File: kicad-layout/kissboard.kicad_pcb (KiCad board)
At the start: 2 copper layers, 132.3 x 103.7 mm, 27 parts, among them J1 Conn_01x04, K1 KEYSW, K10 KEYSW, K11 KEYSW, K12 KEYSW, K13 KEYSW, K14 KEYSW, K15 KEYSW, K16 KEYSW, K17 KEYSW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

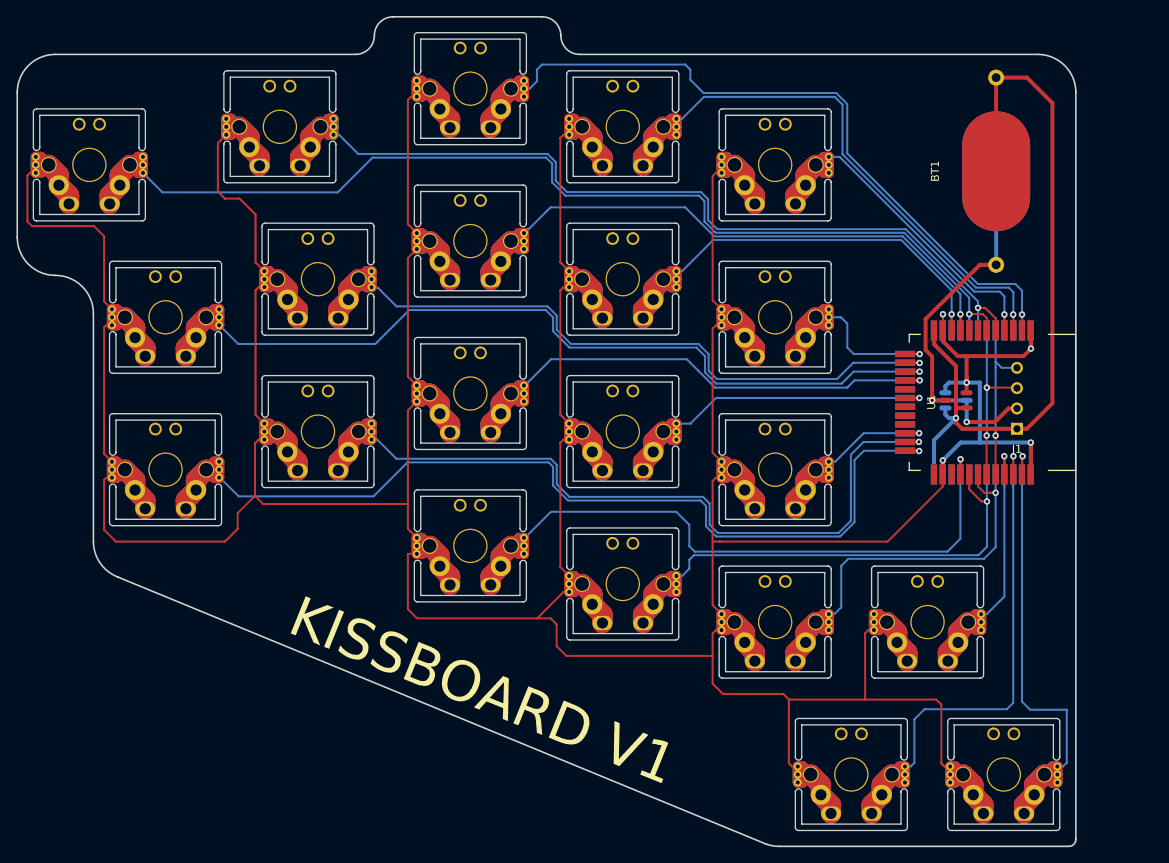
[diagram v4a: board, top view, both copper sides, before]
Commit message: Layout adjusted: lower pinky finger column and straight thumb row
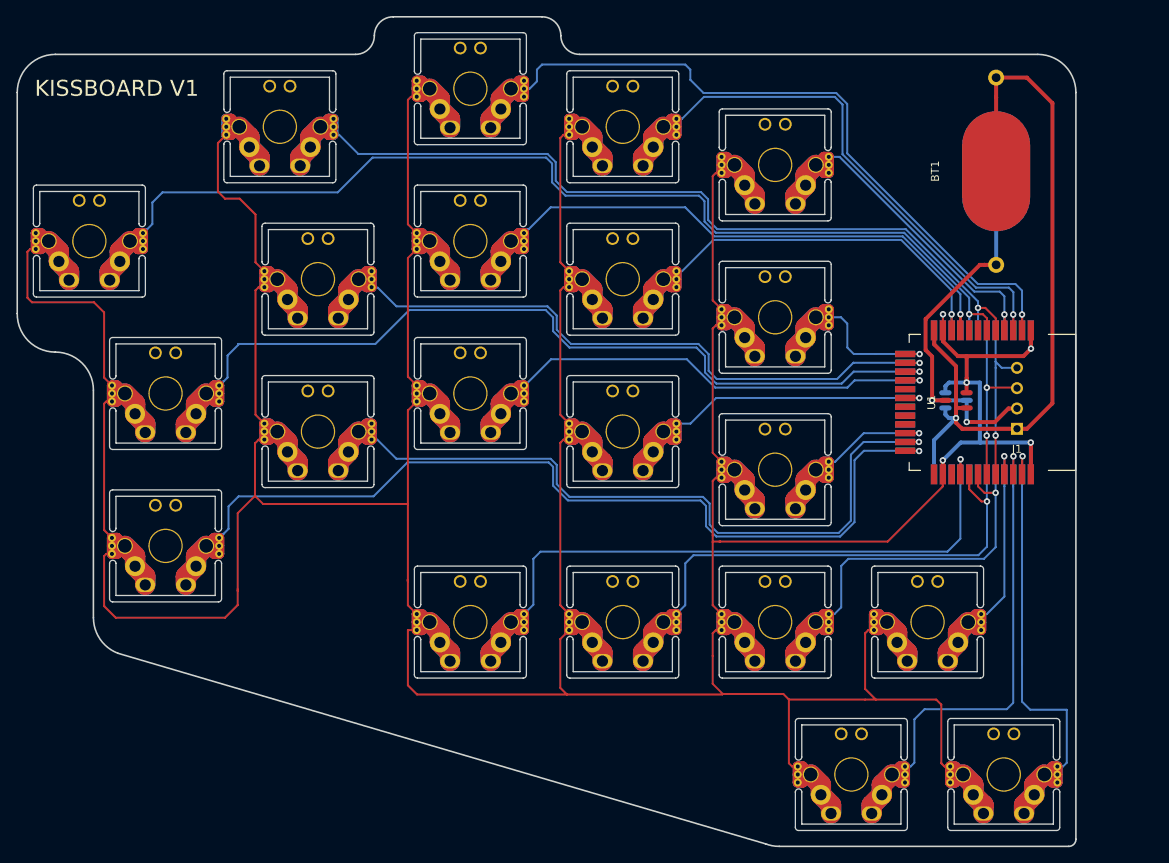
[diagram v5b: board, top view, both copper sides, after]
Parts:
- moved K11 9.53 mm to (52.4, 88.1)
- moved K6 9.53 mm to (52.4, 69.1)
- moved K1 9.52 mm to (42.9, 50.0)
- moved K16 9.52 mm to (90.5, 97.6)
- moved K17 4.76 mm to (109.5, 97.6)
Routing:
- net GND: track 1093.8 -> 1119.8 mm
- net /S17: track 82.0 -> 86.4 mm
- net /S11: track 134.9 -> 137.8 mm
- net /S6: track 125.9 -> 128.8 mm
- net /S1: track 153.5 -> 156.2 mm
- net /S16: track 101.3 -> 103.0 mm
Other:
- outline, holes or cut-outs redrawn

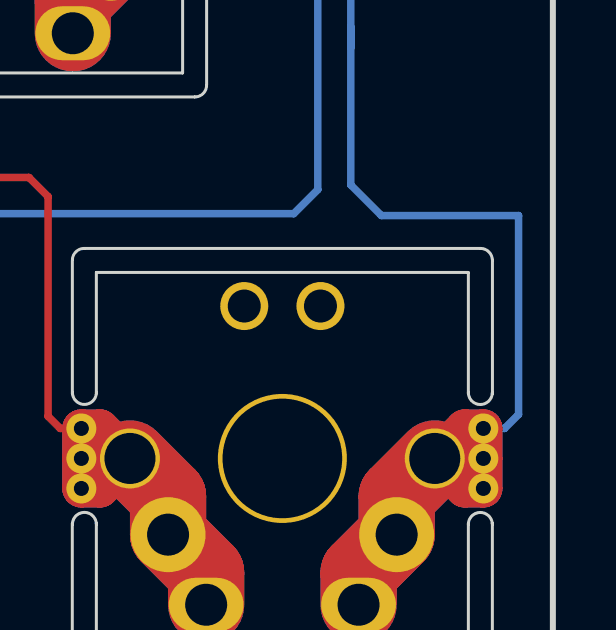
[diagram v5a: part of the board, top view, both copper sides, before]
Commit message: tiny adjustment of a single track
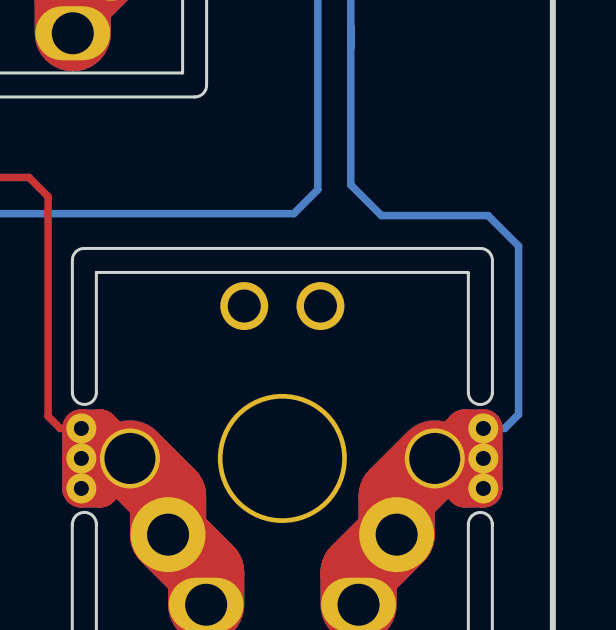
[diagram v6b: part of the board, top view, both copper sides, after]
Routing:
- net /S21: track 74.9 -> 74.3 mm
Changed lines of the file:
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@@
     (thickness 1.6)
     (drawings 21)
-    (tracks 1381)
+    (tracks 1382)
     (zones 0)
     (modules 27)
@@
   (segment (start 154.176998 52.975) (end 154.795787 52.975) (width 0.5) (layer F.Cu) (net 30))
   (segment (start 154.795787 52.975) (end 156.21 52.975) (width 0.5) (layer F.Cu) (net 30))
+  (segment (start 165.0365 109.601) (end 164.0205 108.585) (width 0.25) (layer B.Cu) (net 31))
+  (segment (start 164.0205 108.585) (end 160.4645 108.585) (width 0.25) (layer B.Cu) (net 31))
+  (segment (start 165.0365 115.214356) (end 165.0365 109.601) (width 0.25) (layer B.Cu) (net 31))
   (segment (start 144.86904 68.51396) (end 144.8655 68.5175) (width 0.25) (layer F.Cu) (net 39))
   (segment (start 97.1875 31.95625) (end 96.5675 31.95625) (width 1.27) (layer F.Cu) (net 4))
@@
   (segment (start 160.4645 108.585) (end 159.4435 107.564) (width 0.25) (layer B.Cu) (net 31))
   (segment (start 159.4435 107.564) (end 159.4435 102.2985) (width 0.25) (layer B.Cu) (net 31))
-  (segment (start 165.0365 108.585) (end 160.4645 108.585) (width 0.25) (layer B.Cu) (net 31))
-  (segment (start 165.0365 115.214356) (end 165.0365 108.585) (width 0.25) (layer B.Cu) (net 31))
   (segment (start 163.8625 115.68125) (end 164.569606 115.68125) (width 0.25) (layer B.Cu) (net 31))
   (segment (start 164.569606 115.68125) (end 165.0365 115.214356) (width 0.25) (layer B.Cu) (net 31))

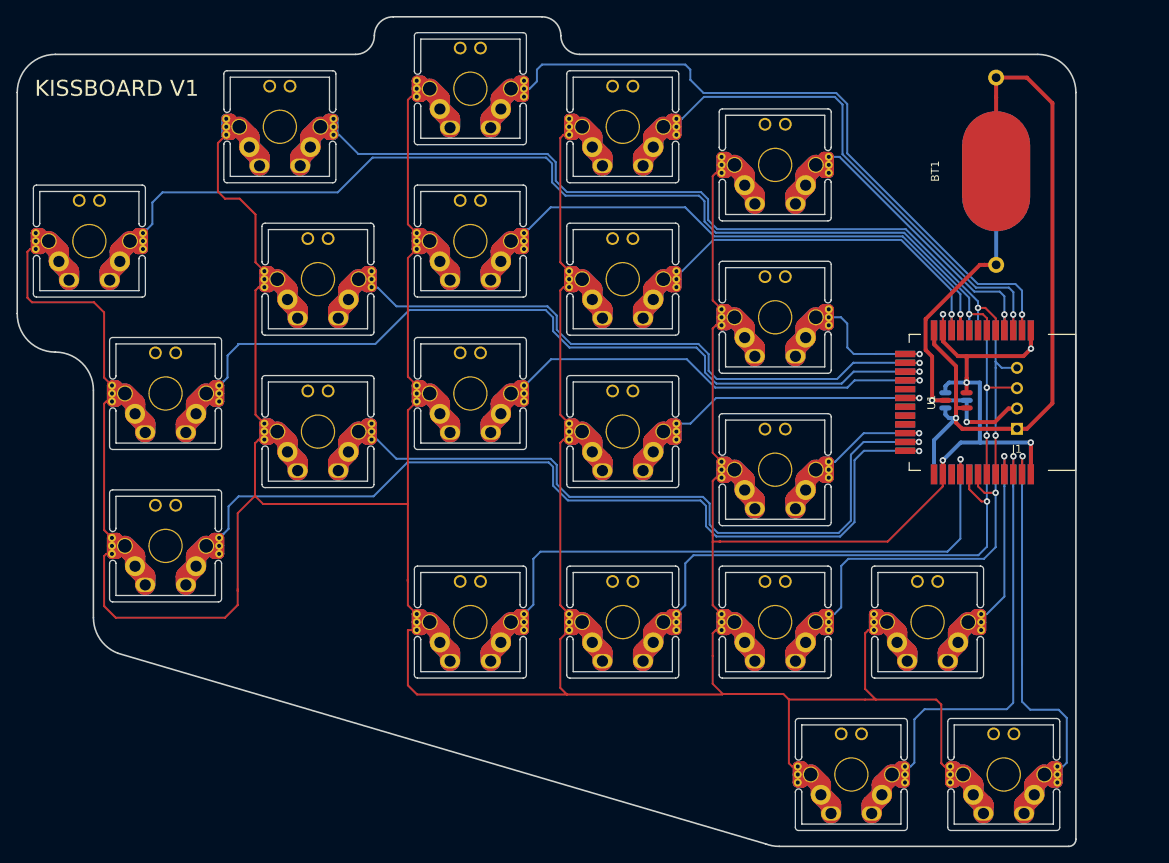
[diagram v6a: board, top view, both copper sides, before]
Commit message: Fixed thumb row: moved half key in towards thumb
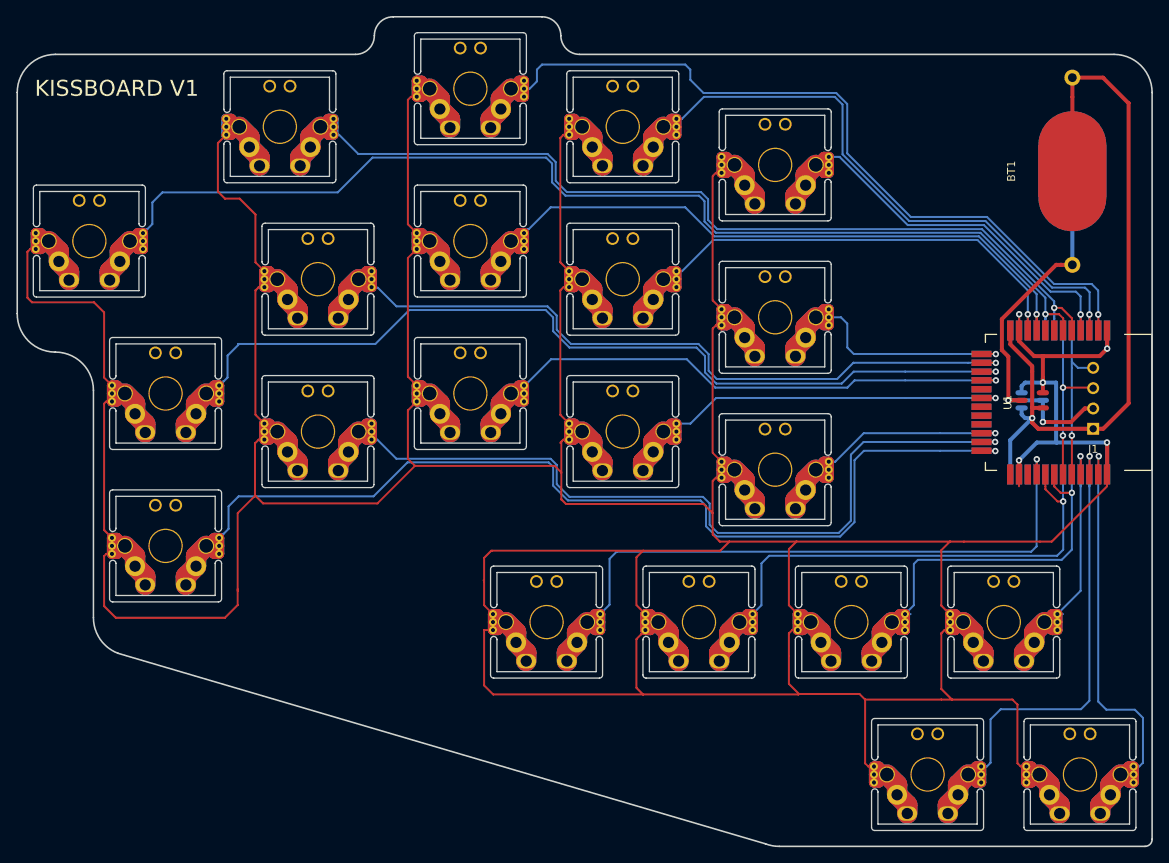
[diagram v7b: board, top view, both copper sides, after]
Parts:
- moved BT1 9.53 mm to (165.7, 41.3)
- moved J1 9.53 mm to (168.3, 73.5)
- moved K16 9.53 mm to (100.0, 97.6)
- moved K17 9.53 mm to (119.1, 97.6)
- moved K18 9.53 mm to (138.1, 97.6)
- moved K19 9.53 mm to (157.2, 97.6)
- moved K21 9.53 mm to (166.7, 116.7)
- moved Q1 9.53 mm to (160.7, 69.9)
- moved Q2 9.53 mm to (160.7, 69.9)
- moved K20 9.52 mm to (147.6, 116.7)
- moved U1 9.52 mm to (165.3, 70.2)
- moved U2 9.52 mm to (165.3, 70.2)
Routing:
- net GND: track 1119.8 -> 1206.9 mm
- net /S1: track 156.2 -> 165.7 mm
- net /S7: track 105.4 -> 114.9 mm
- net /S8: track 96.2 -> 105.7 mm
- net /S3: track 116.7 -> 126.2 mm
- net /S14: track 60.7 -> 70.2 mm
- net /S13: track 81.9 -> 91.4 mm
- net /S12: track 114.7 -> 124.3 mm
- net /S10: track 44.0 -> 53.6 mm
- net /S5: track 62.7 -> 72.2 mm
- net /S9: track 72.9 -> 82.4 mm
- net /S6: track 128.8 -> 138.3 mm
- net /S2: track 128.0 -> 137.6 mm
- net /S11: track 137.8 -> 147.4 mm
- net /S15: track 41.8 -> 51.3 mm
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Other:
- board size 132.3 x 103.7 mm -> 141.9 x 103.7 mm
